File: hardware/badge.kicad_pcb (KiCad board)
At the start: 2 copper layers, 88 x 115 mm, 130 parts, among them J2 MY-18650-01, J3 Conn_01x40, J4 USB_C_Receptacle_USB2.0_14P, J5 MY-18650-01, J6 Micro_SD_Card_Det1, Q1 AO3400A, Q3 AO3400A, SW1 SW_Push, SW10 SW_Push, SW11 SW_Push, SW12 SW_Push, SW13 SW_Push, SW14 SW_Push, SW15 SW_Push, SW16 SW_Push, SW17 SW_Push, SW18 SW_Push, SW19 SW_Push, SW2 SW_Push, SW20 SW_Push, SW21 SW_Push, SW22 SW_Push, SW23 SW_Push, SW24 BOOT, SW25 SW_Push, SW26 SW_Push, SW27 SW_Push, SW28 SW_Push, SW29 SW_Push, SW3 SW_Push, SW30 SW_Push, SW31 SW_Push, SW33 SW_Push, SW34 SW_Push, SW35 SW_Push, SW36 SW_Push, SW37 SW_Push, SW38 SW_Push, SW39 SW_Push, SW4 SW_Push, SW5 SW_Push, SW57 MK-12C02-G020, SW58 SKRHABE010, SW6 SW_Push, SW7 SW_Push, SW8 RST, SW9 SW_Push, U1 ESP32-S3-WROOM-1, U11 PCA9555PW, U2 Ai-Thinker-Ra-02, U3 BQ24075RGT, U4 TLV62569DBV, U5 BME280, U6 USBLC6-2P6, U7 BMI270, U9 MAX98357A

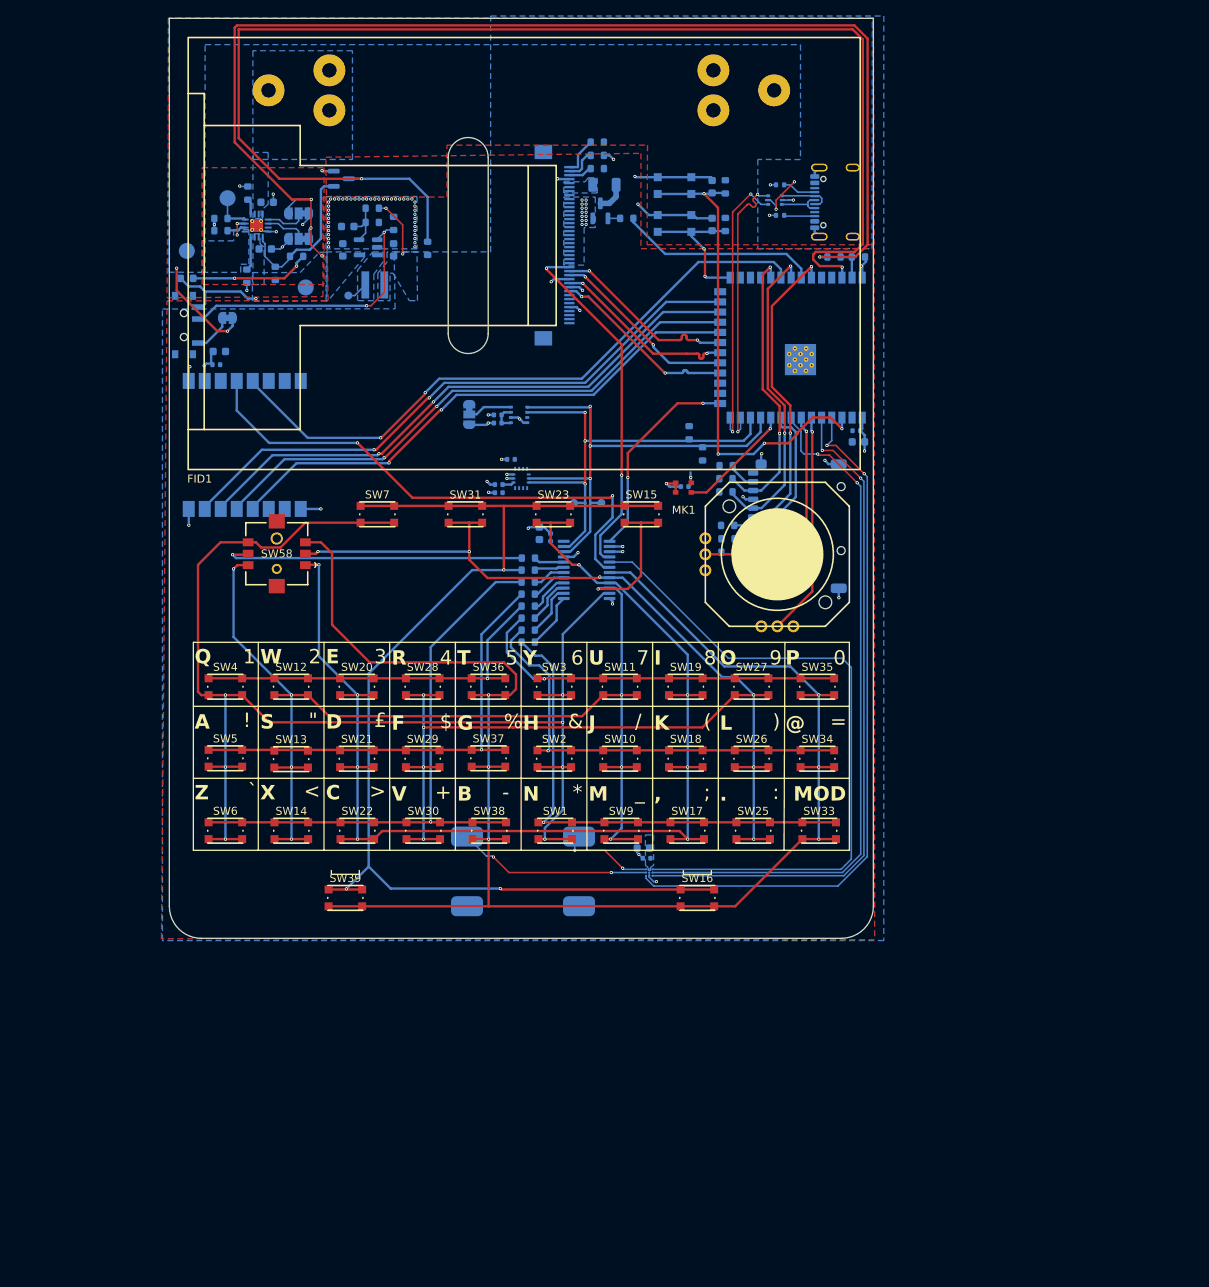
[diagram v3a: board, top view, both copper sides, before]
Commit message: Fix via anular ring
Fix position of colliding components
Add mic pin 1 marker manually
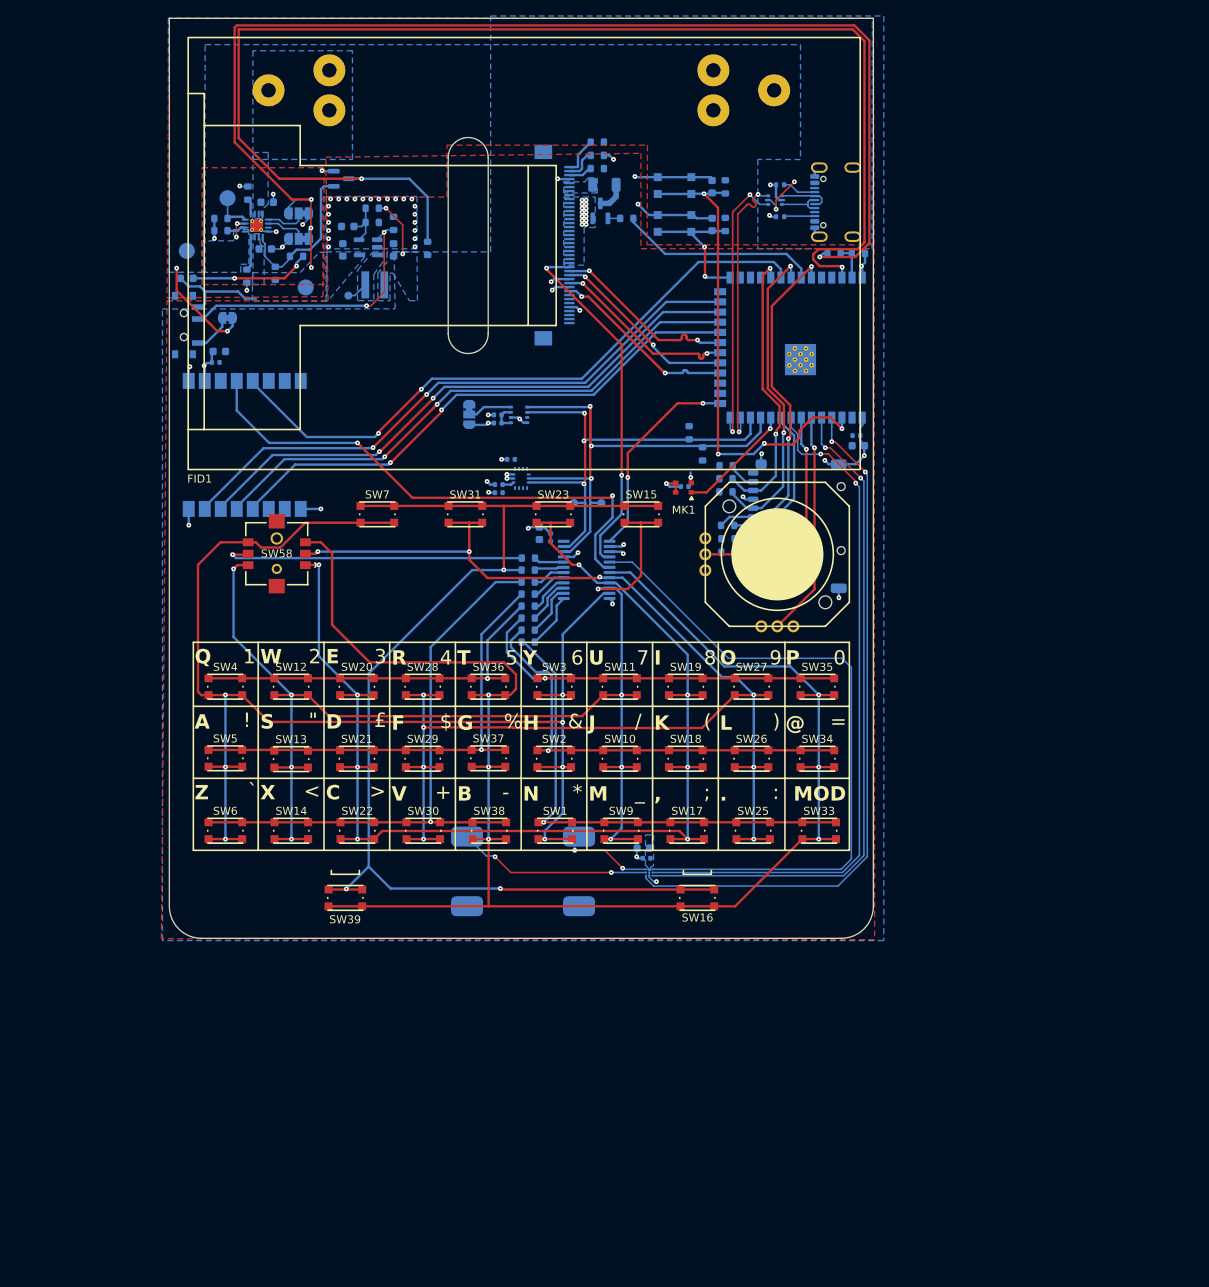
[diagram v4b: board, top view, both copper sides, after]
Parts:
- moved C19 0.61 mm to (166.9, 83.2)
- moved C18 0.48 mm to (167.1, 84.4)
- moved R33 0.43 mm to (167.1, 60.4)
- moved R34 0.43 mm to (164.1, 60.4)
- moved C12 0.29 mm to (86.8, 74.0)
- moved R27 0.18 mm to (157.4, 55.8)
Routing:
- net GND: track 103.0 -> 110.4 mm, vias 104 -> 81
- net +3.3V: track 15.0 -> 19.5 mm
- net VSYS: track 166.7 -> 168.0 mm, vias 5 -> 4
- net /AUDIO.LRCLK: track 87.8 -> 86.9 mm
- net /mcu/SD_CS: track 21.2 -> 20.3 mm
- net /mcu/VBAT_DIV2: track 3.99 -> 4.59 mm
